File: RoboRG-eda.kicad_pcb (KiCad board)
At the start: 4 copper layers, 50 x 100 mm, 80 parts, among them J1 USB_C_Receptacle_USB2.0, J2 AudioJack3_Switch, J3 connector-pan, J4 connector-tilt, J5 connector-other, J6 USB_C_Receptacle_USB2.0, J7 SWD, J8 USART, J9 Barrel_Jack_Switch, Q1 Q_PNP_BEC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

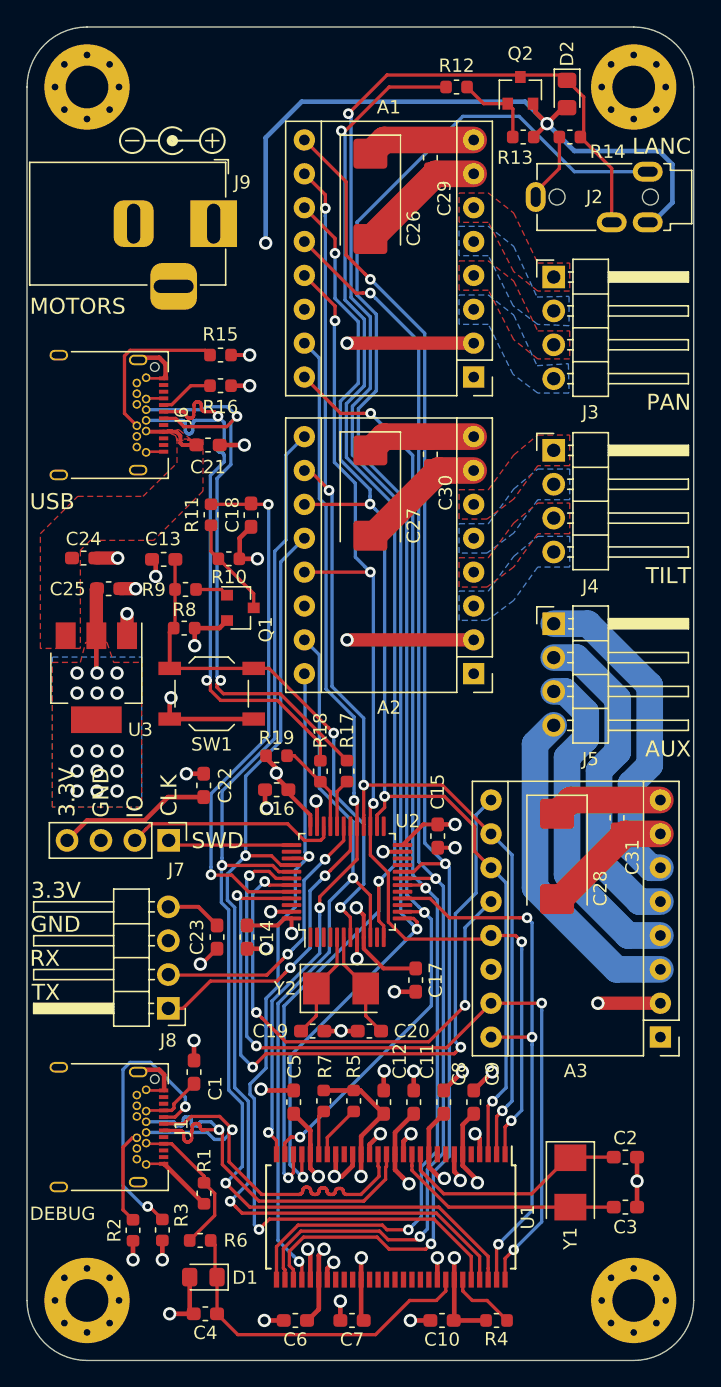
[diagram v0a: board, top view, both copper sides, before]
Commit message: Propagate all fixes to the PCB
Also fix some footprints along the way.
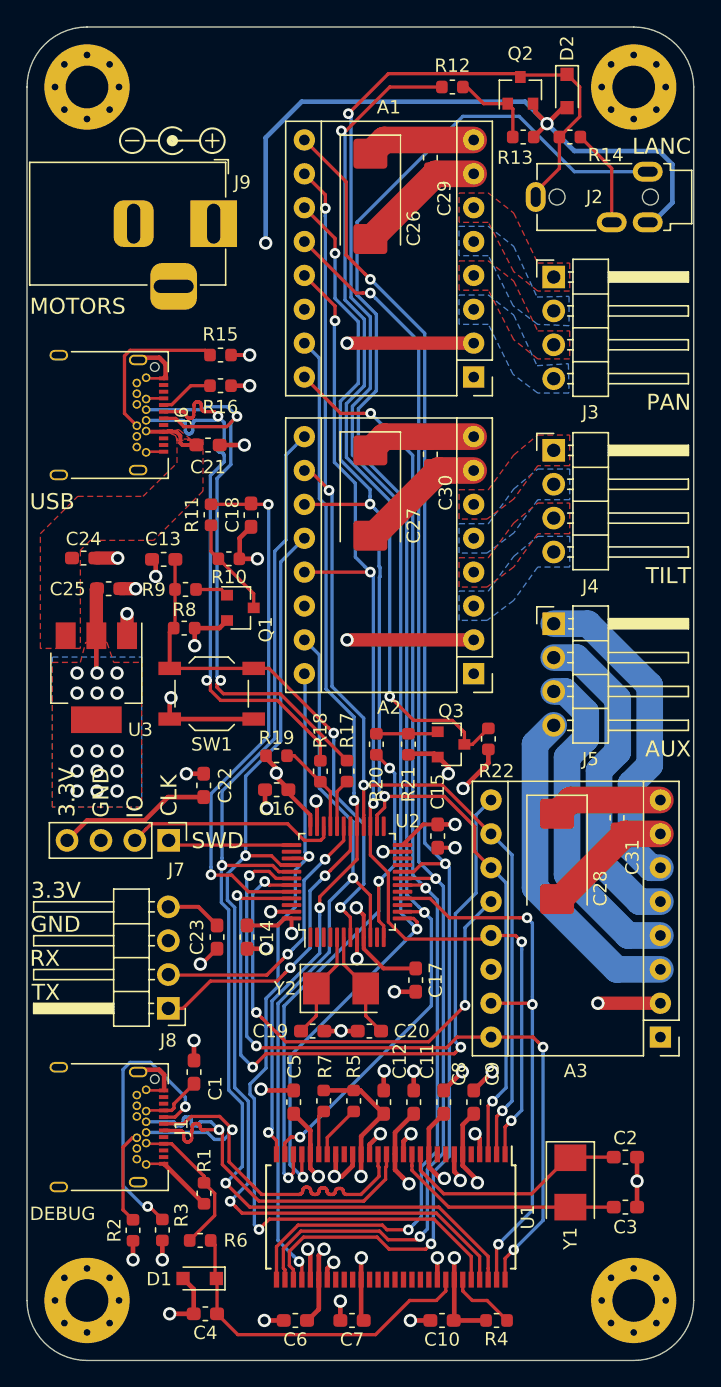
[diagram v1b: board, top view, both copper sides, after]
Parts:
- added Q3: Q_NPN_BEC, Package_TO_SOT_SMD:SOT-23, F.Cu at (131.8, 103.8)
- added R20: 1kΩ, Resistor_SMD:R_0603_1608Metric, F.Cu at (126.2, 103.8)
- added R21: 10kΩ, Resistor_SMD:R_0603_1608Metric, F.Cu at (128.6, 103.8)
- added R22: 1kΩ, Resistor_SMD:R_0603_1608Metric, F.Cu at (134.6, 103.4)
- D1, D2: footprint Diode_SMD:D_0805_2012Metric_Pad1.15x1.40mm_HandSolder -> Diode_SMD:D_SOD-323_HandSoldering
- moved R12 0.31 mm to (131.9, 54.5)
- moved D1 0.29 mm to (113.0, 143.8)
- moved D2 0.23 mm to (140.5, 54.8)
- turned R14 to 180 degrees
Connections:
- A3 pad 15: dir-other -> step-other
- A3 pad 16: step-other -> dir-other
- J2 pad R: LANC-in -> Net-(J2-PadR)
- J2 pad T: Net-(J2-PadT) -> LANC-in
- R12 pad 2: LANC-out -> Net-(Q3-Pad3)
- R14 pad 1: Net-(J2-PadT) -> Net-(J2-PadR)
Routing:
- net Net-(Q3-Pad3): track 0.00 -> 63.8 mm, vias 0 -> 2
- net LANC-out: track 100.3 -> 42.1 mm
- net Net-(J2-PadR): track 0.00 -> 7.37 mm
- net Net-(J2-PadT): track 5.24 -> 0.00 mm
- net Net-(Q3-Pad1): track 0.00 -> 4.66 mm
- net GND: track 208.5 -> 212.6 mm, vias 43 -> 44
- net dir-other: track 61.4 -> 57.5 mm
- net +3V3: track 125.8 -> 129.6 mm, vias 31 -> 32
- net LANC-in: track 121.0 -> 119.6 mm

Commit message: Proper page settings for the PCB
Also bump the version to 1.0.1.
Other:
- board text added: "1.0.1"
- board text removed: "1.0.0"
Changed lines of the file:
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@@
   )
   (page A4 portrait)
+  (title_block
+    (title "RoboRG Camera Motion Control System")
+    (date 2019-05-13)
+    (rev 1.0.1)
+    (company RGVID.EU)
+    (comment 1 "Licensed under GNU AGPLv3 or any later version of the license")
+    (comment 2 "    Aleks-Daniel Jakimenko-Aleksejev <alex.jakimenko@gmail.com>")
+    (comment 3 "Copyright © 2018-2019")
+    (comment 4 "This file is part of RoboRG")
+  )
   (layers
     (0 F.Cu signal)
@@
     (effects (font (size 1.5 1.5) (thickness 0.3)) (justify mirror))
   )
-  (gr_text 1.0.0 (at 123.9 77.75 270) (layer B.SilkS)
+  (gr_text 1.0.1 (at 123.9 77.75 270) (layer B.SilkS)
     (effects (font (size 2 2) (thickness 0.3)) (justify mirror))
   )
@@
   (segment (start 128.1625 116.85) (end 128.983741 116.85) (width 0.25) (layer F.Cu) (net 26))
   (segment (start 128.983741 116.85) (end 129.250001 117.11626) (width 0.25) (layer F.Cu) (net 26))
-  (segment (start 143.85 64.65) (end 143.85 60.6) (width 0.25) (layer F.Cu) (net 99) (status 10))
-  (segment (start 143.85 60.6) (end 141.5 58.25) (width 0.25) (layer F.Cu) (net 99) (status 20))
   (segment (start 139.925 60.6) (end 138.15 62.375) (width 0.25) (layer F.Cu) (net 26) (status 20))
   (segment (start 139.925 58.25) (end 139.925 60.6) (width 0.25) (layer F.Cu) (net 26) (status 10))
@@
   (segment (start 126.75 117.403542) (end 126.37498 117.028522) (width 0.25) (layer F.Cu) (net 45))
   (segment (start 126.37498 117.028522) (end 126.37498 114.06302) (width 0.25) (layer F.Cu) (net 45))
-  (via (at 123.574979 57.787473) (size 0.8) (drill 0.4) (layers F.Cu B.Cu) (net 100))
-  (segment (start 123.952756 78.251424) (end 125.300011 76.904169) (width 0.25) (layer B.Cu) (net 100))
-  (segment (start 123.952756 82.275578) (end 123.952756 78.251424) (width 0.25) (layer B.Cu) (net 100))
-  (segment (start 127.2 85.522822) (end 123.952756 82.275578) (width 0.25) (layer B.Cu) (net 100))
-  (segment (start 125.300011 71.920835) (end 123.850011 70.470835) (width 0.25) (layer B.Cu) (net 100))
-  (segment (start 127.2 100.2) (end 127.2 85.522822) (width 0.25) (layer B.Cu) (net 100))
-  (segment (start 125.300011 76.904169) (end 125.300011 71.920835) (width 0.25) (layer B.Cu) (net 100))
-  (segment (start 123.850011 70.470835) (end 123.850011 58.062505) (width 0.25) (layer B.Cu) (net 100))
-  (segment (start 123.850011 58.062505) (end 123.574979 57.787473) (width 0.25) (layer B.Cu) (net 100))
-  (via (at 127.2 100.2) (size 0.8) (drill 0.4) (layers F.Cu B.Cu) (net 100))
   (via (at 127.2 105.575004) (size 0.8) (drill 0.4) (layers F.Cu B.Cu) (net 45))
   (segment (start 127.2 105.575) (end 127.2 105.575004) (width 0.25) (layer F.Cu) (net 45))
@@
   (segment (start 113.425001 78.474999) (end 115.025001 78.474999) (width 0.25) (layer B.Cu) (net 98))
   (segment (start 113.2 78.7) (end 113.425001 78.474999) (width 0.25) (layer B.Cu) (net 98))
+  (segment (start 143.85 64.65) (end 143.85 60.6) (width 0.25) (layer F.Cu) (net 99) (status 10))
+  (segment (start 143.85 60.6) (end 141.5 58.25) (width 0.25) (layer F.Cu) (net 99) (status 20))
+  (via (at 123.574979 57.787473) (size 0.8) (drill 0.4) (layers F.Cu B.Cu) (net 100))
+  (segment (start 123.952756 78.251424) (end 125.300011 76.904169) (width 0.25) (layer B.Cu) (net 100))
+  (segment (start 123.952756 82.275578) (end 123.952756 78.251424) (width 0.25) (layer B.Cu) (net 100))
+  (segment (start 127.2 85.522822) (end 123.952756 82.275578) (width 0.25) (layer B.Cu) (net 100))
+  (segment (start 125.300011 71.920835) (end 123.850011 70.470835) (width 0.25) (layer B.Cu) (net 100))
+  (segment (start 127.2 100.2) (end 127.2 85.522822) (width 0.25) (layer B.Cu) (net 100))
+  (segment (start 125.300011 76.904169) (end 125.300011 71.920835) (width 0.25) (layer B.Cu) (net 100))
+  (segment (start 123.850011 70.470835) (end 123.850011 58.062505) (width 0.25) (layer B.Cu) (net 100))
+  (segment (start 123.850011 58.062505) (end 123.574979 57.787473) (width 0.25) (layer B.Cu) (net 100))
+  (via (at 127.2 100.2) (size 0.8) (drill 0.4) (layers F.Cu B.Cu) (net 100))
   (segment (start 123.574979 57.787473) (end 123.912527 57.787473) (width 0.25) (layer F.Cu) (net 100))
   (segment (start 127.2 54.5) (end 131.1125 54.5) (width 0.25) (layer F.Cu) (net 100))

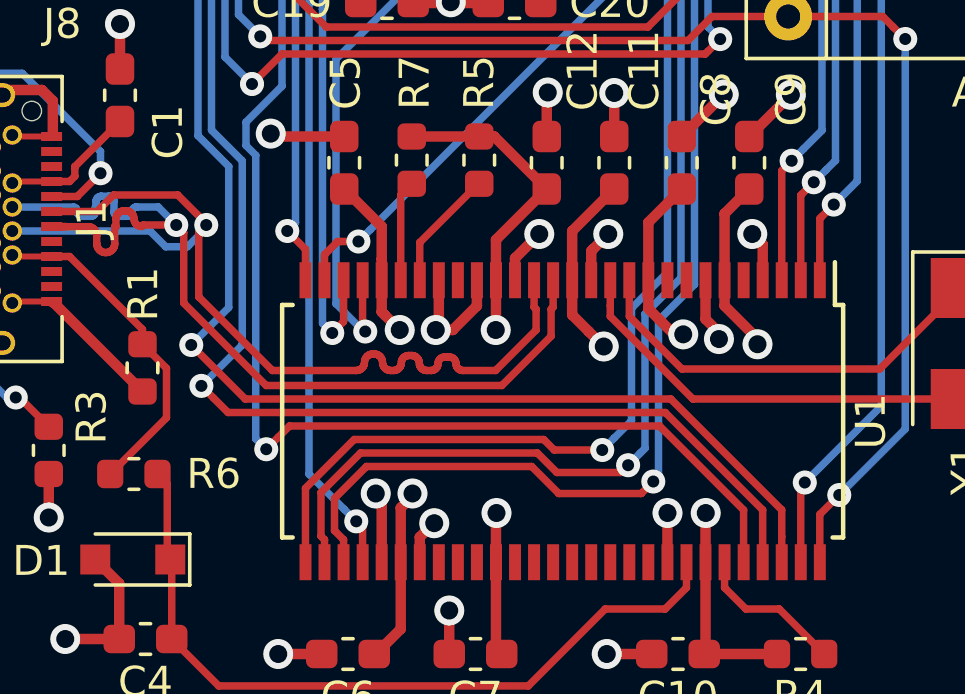
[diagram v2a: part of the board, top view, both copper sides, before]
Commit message: Flip D+/D- of the LA
Oops!
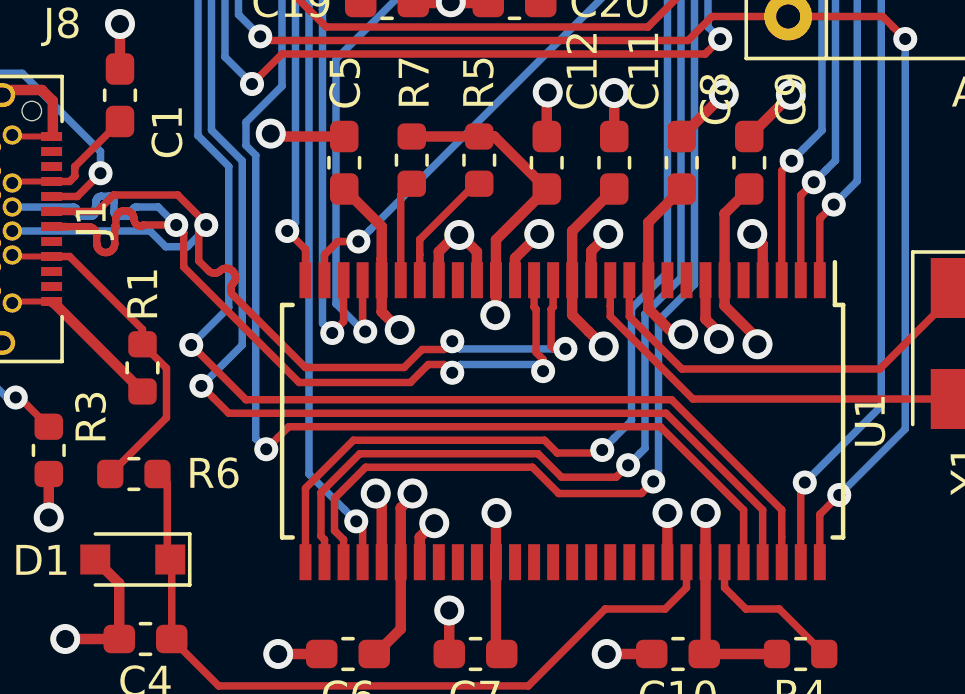
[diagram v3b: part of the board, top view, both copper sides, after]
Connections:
- U1 pad 15: /Optional/USB-LA-D- -> /Optional/USB-LA-D+
- U1 pad 16: /Optional/USB-LA-D+ -> /Optional/USB-LA-D-
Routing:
- net GND: track 212.6 -> 212.0 mm
- net /Optional/USB-LA-D-: track 32.5 -> 32.6 mm, vias 1 -> 3
- net /Optional/USB-LA-D+: track 31.6 -> 31.7 mm, vias 1 -> 3
